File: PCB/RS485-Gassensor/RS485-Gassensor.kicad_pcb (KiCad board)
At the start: 2 copper layers, 92 x 46 mm, 66 parts, among them J1 Screw_Terminal_01x08, J2 Screw_Terminal_01x04, J3 Screw_Terminal_01x08, J4 Screw_Terminal_01x06, J5 Screw_Terminal_01x06, SW1 SW_DIP_x06, U1 STM32G031K8Tx, U2 STM32G031K8Ux, U3 MQ-6, U4 OKI-78SR-5_1.5-W36-C, U5 AP2127N-3.3, U6 AD8676xR, U7 LT1785xS8, U8 MQ-6, U9 AD8676xR

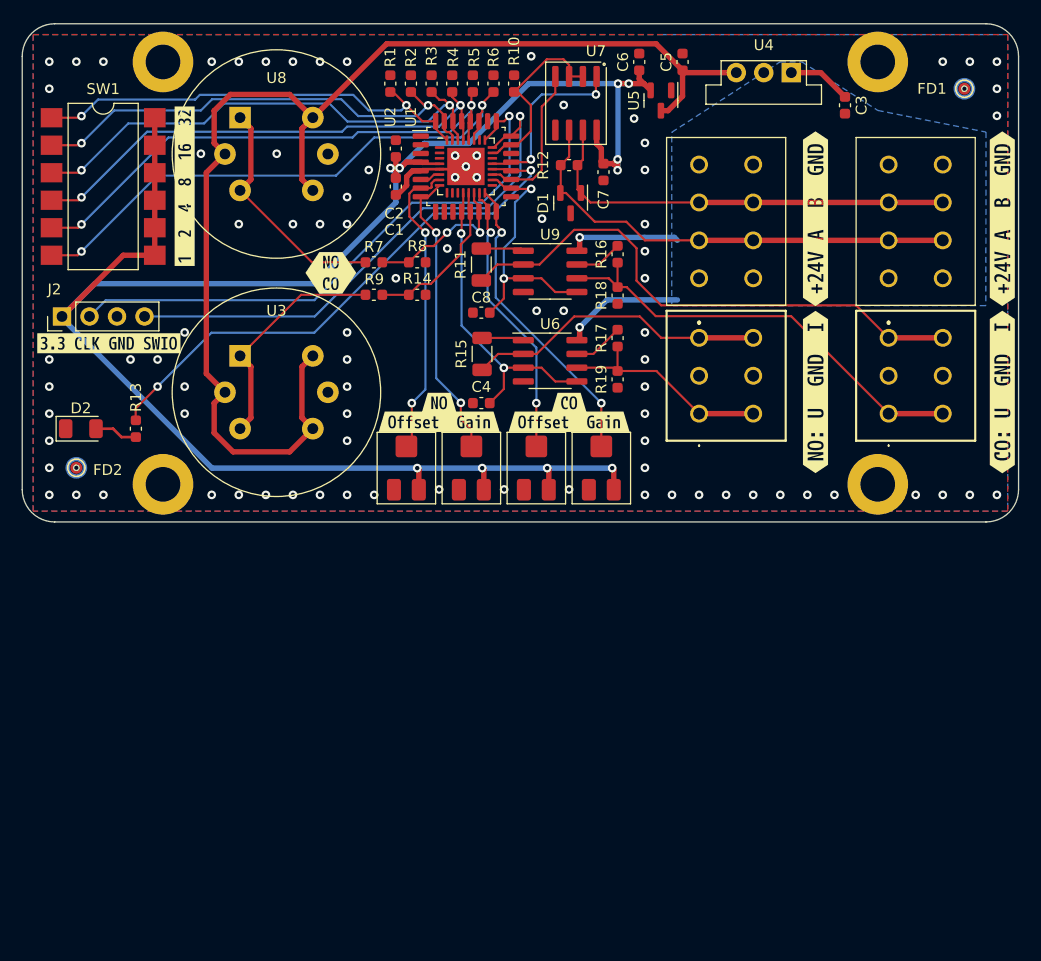
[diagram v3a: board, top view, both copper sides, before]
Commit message: imoproved filter
one dual channel Op amp, corrections from first produced prototype
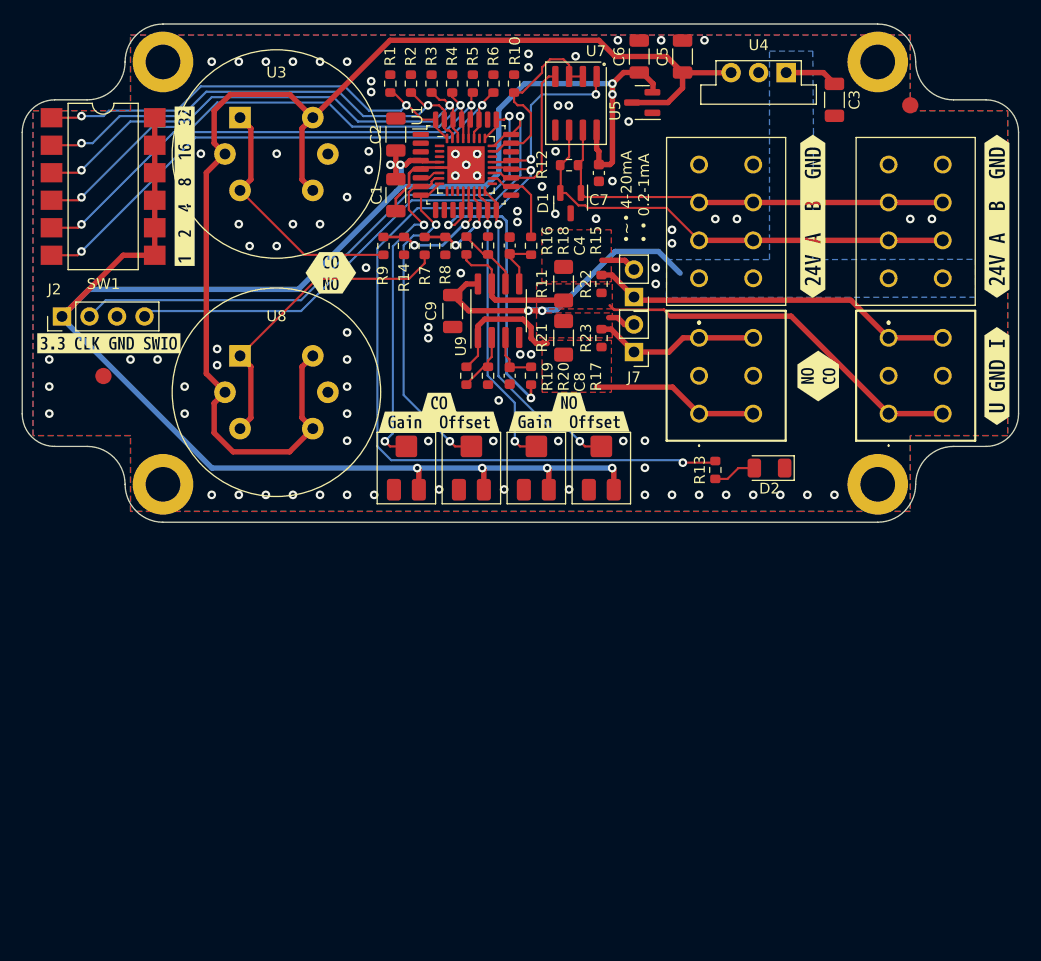
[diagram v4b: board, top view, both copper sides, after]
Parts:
- removed FD1, FD2: ~, Custom_Library:Alignement_Testpoint_2Layer
- removed U6: AD8676xR, Package_SO:SOIC-8_3.9x4.9mm_P1.27mm
- removed kibuzzard-64E927CD: G***, kibuzzard-64E927CD
- removed kibuzzard-64E9307C (x2): G***, kibuzzard-64E9307C
- removed kibuzzard-64E930E3: G***, kibuzzard-64E930E3
- removed kibuzzard-64E93122: G***, kibuzzard-64E93122
- removed kibuzzard-64E95911 (x2): G***, kibuzzard-64E95911
- added C9: CAP1uF, Capacitor_SMD:C_1206_3216Metric, F.Cu at (169.8, 45.5)
- added FID1: Fiducial, Fiducial:Fiducial_1.5mm_Mask3mm, F.Cu at (137.5, 51.5)
- added FID2: Fiducial, Fiducial:Fiducial_1.5mm_Mask3mm, F.Cu at (212.0, 26.5)
- added J6: Conn_01x02_Pin, Connector_PinHeader_2.54mm:PinHeader_1x02_P2.54mm_Vertical, F.Cu at (186.5, 44.2)
- added J7: Conn_01x02_Pin, Connector_PinHeader_2.54mm:PinHeader_1x02_P2.54mm_Vertical, F.Cu at (186.5, 49.3)
- added R20: R1K, Resistor_SMD:R_0603_1608Metric, F.Cu at (173.0, 51.5)
- added R21: R470, Resistor_SMD:R_1206_3216Metric_Pad1.30x1.75mm_HandSolder, F.Cu at (180.0, 48.0)
- added R22: 10KR, Resistor_SMD:R_0603_1608Metric, F.Cu at (183.5, 43.0)
- added R23: 10KR, Resistor_SMD:R_0603_1608Metric, F.Cu at (183.5, 48.0)
- added kibuzzard-64EB9F88: G***, kibuzzard-64EB9F88, F.Cu at (158.5, 42.0)
- added kibuzzard-64ECCA5B: G***, kibuzzard-64ECCA5B, F.Cu at (203.0, 36.8)
- added kibuzzard-64ECCA80: G***, kibuzzard-64ECCA80, F.Cu at (220.0, 36.8)
- added kibuzzard-64ECCBAE: G***, kibuzzard-64ECCBAE, F.Cu at (220.0, 51.5)
- added kibuzzard-650224BF: G***, kibuzzard-650224BF, F.Cu at (168.5, 55.7)
- added kibuzzard-650224CC: G***, kibuzzard-650224CC, F.Cu at (180.5, 55.7)
- added kibuzzard-650224F1: G***, kibuzzard-650224F1, F.Cu at (203.5, 51.5)
- C1, C2, C6: footprint Capacitor_SMD:C_0603_1608Metric -> Capacitor_SMD:C_1206_3216Metric
- C3: value CAP2.2uF -> CAP10uF; footprint Capacitor_SMD:C_0603_1608Metric -> Capacitor_SMD:C_1206_3216Metric
- C4, C8: value CAP100nF -> 470nF
- C5: value CAP2.2uF -> CAP22uF; footprint Capacitor_SMD:C_0603_1608Metric -> Capacitor_SMD:C_1206_3216Metric
- R1, R10, R12, R13, R14, R18, R2, R3, R4, R5, R6, R7, R8, R9: footprint Capacitor_SMD:C_0603_1608Metric -> Resistor_SMD:R_0603_1608Metric
- R11: value R150 -> R470; footprint Capacitor_SMD:C_1206_3216Metric -> Resistor_SMD:R_1206_3216Metric_Pad1.30x1.75mm_HandSolder
- R15: value R150 -> 1k; footprint Capacitor_SMD:C_1206_3216Metric -> Resistor_SMD:R_0603_1608Metric
- R16, R19: value R1K -> 2.2k; footprint Capacitor_SMD:C_0603_1608Metric -> Resistor_SMD:R_0603_1608Metric
- R17: value R1K -> 1k; footprint Capacitor_SMD:C_0603_1608Metric -> Resistor_SMD:R_0603_1608Metric
- U9: value AD8676xR -> AD8676
- moved D2 63.7 mm to (199.0, 60.0), turned to 180 degrees
- moved R13 53.6 mm to (194.0, 60.2)
- moved U3 22.0 mm to (150.1, 27.6)
- moved U8 22.0 mm to (150.1, 49.6)
- moved C4 14.8 mm to (175.0, 39.4), turned to 90 degrees
- moved R16 14.0 mm to (171.0, 39.4), turned to 90 degrees
- moved R19 14.0 mm to (171.0, 51.5)
- moved R18 12.8 mm to (173.0, 39.4), turned to 90 degrees
- moved kibuzzard-64E958EB 12.0 mm to (180.5, 54.0)
- moved kibuzzard-64E958FD 12.0 mm to (168.5, 54.0)
- moved R15 11.0 mm to (177.0, 39.5)
- moved R17 8.71 mm to (177.0, 51.5), turned to 90 degrees
- moved R11 7.80 mm to (180.0, 43.0), turned to 90 degrees
- moved C8 6.39 mm to (175.0, 51.5), turned to -90 degrees
- moved U9 5.99 mm to (174.0, 45.5), turned to 90 degrees
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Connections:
- net /CO renamed CO
- net /DIP0 renamed DIP0
- net /DIP1 renamed DIP1
- net /DIP2 renamed DIP2
- net /DIP3 renamed DIP3
- net /DIP4 renamed DIP4
- net /DIP5 renamed DIP5
- net /Gain_CO renamed Gain_CO
- net /Gain_NO renamed Gain_NO
- net /LED renamed LED
- net /NO2 renamed NO2
- net /RS485-A renamed RS485-A
- net /RS485-B renamed RS485-B
- net /Read_!Enable renamed Read_!Enable
- net /SWCLK renamed SWCLK
- net /SWDIO renamed SWDIO
- net /T_NRST-Button renamed T_NRST-Button
- net /UART_RX renamed UART_RX
- net /UART_TX renamed UART_TX
- net /offset_CO renamed offset_CO
- net /offset_NO renamed offset_NO
- C4 pad 1: /analog_PWM_NO -> Net-(U9B-+)
- C8 pad 1: /analog_PWM_CO -> Net-(U9A-+)
- J4 pad 1: /U_Out_NO -> U_Out_NO
- J4 pad 2: /U_Out_NO -> U_Out_NO
- J4 pad 5: /I_Out_NO -> I_Out_NO
- J4 pad 6: /I_Out_NO -> I_Out_NO
- J5 pad 1: /U_Out_CO -> U_Out_CO
- J5 pad 2: /U_Out_CO -> U_Out_CO
- J5 pad 5: /I_Out_CO -> I_Out_CO
- J5 pad 6: /I_Out_CO -> I_Out_CO
- R11 pad 1: Net-(R11-Pad1) -> U_Out_CO
- R11 pad 2: /I_Out_CO -> Net-(J6-Pin_2)
- R15 pad 1: Net-(R15-Pad1) -> analog_PWM_CO
- R15 pad 2: /I_Out_NO -> Net-(U9B-+)
- R16 pad 1: Net-(R16-Pad1) -> U_Out_CO
- R16 pad 2: /U_Out_CO -> Net-(U9B--)
- R17 pad 1: Net-(R17-Pad1) -> analog_PWM_NO
- R17 pad 2: /U_Out_NO -> Net-(U9A-+)
- R18 pad 1: /U_Out_CO -> Net-(U9B--)
- R19 pad 1: /U_Out_NO -> U_Out_NO
- R19 pad 2: GND -> Net-(U9A--)
- U1 pad 12: /analog_PWM_NO -> analog_PWM_NO
- U1 pad 18: /analog_PWM_CO -> analog_PWM_CO
- U2 pad 12: /analog_PWM_NO -> analog_PWM_NO
- U2 pad 18: /analog_PWM_CO -> analog_PWM_CO
- U9 pad 1: Net-(R11-Pad1) -> U_Out_NO
- U9 pad 2: /I_Out_CO -> Net-(U9A--)
- U9 pad 3: /analog_PWM_CO -> Net-(U9A-+)
- U9 pad 5: /analog_PWM_CO -> Net-(U9B-+)
- U9 pad 6: /U_Out_CO -> Net-(U9B--)
- U9 pad 7: Net-(R16-Pad1) -> U_Out_CO
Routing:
- net /I_Out_CO: track 50.4 -> 0.00 mm
- net U_Out_CO: track 0.00 -> 47.5 mm
- net /U_Out_CO: track 41.2 -> 0.00 mm
- net I_Out_CO: track 0.00 -> 33.9 mm
- net /analog_PWM_NO: track 28.9 -> 0.00 mm, vias 2 -> 0
- net analog_PWM_NO: track 0.00 -> 28.4 mm, vias 0 -> 2
- net U_Out_NO: track 0.00 -> 28.0 mm
- net /I_Out_NO: track 27.9 -> 0.00 mm
- net /analog_PWM_CO: track 24.4 -> 0.00 mm, vias 2 -> 0
- net LED: track 50.6 -> 71.2 mm
- net /U_Out_NO: track 20.3 -> 0.00 mm
- net I_Out_NO: track 0.00 -> 15.4 mm
- net analog_PWM_CO: track 0.00 -> 7.51 mm
- net Net-(U8-B1): track 21.9 -> 28.9 mm
- net Net-(U9B--): track 0.00 -> 6.08 mm
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- added copper zone on F.Cu, net Net-(J6-Pin_2)
- added copper zone on F.Cu, net Net-(J7-Pin_2)
- added copper zone on F.Cu, net U_Out_CO
- added copper zone on F.Cu, net U_Out_NO
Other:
- outline, holes or cut-outs redrawn
- board text added: "PROTOTYPE V2 Garage Gas Sensor Felix Sarbach 2023"
- board text added: "•~• 4-20mA • • 0.2-1mA"
- board text removed: "PROTOTYPE V1 Garage Gas Sensor Felix Sarbach 2023"

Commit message: added Modbus / RS485
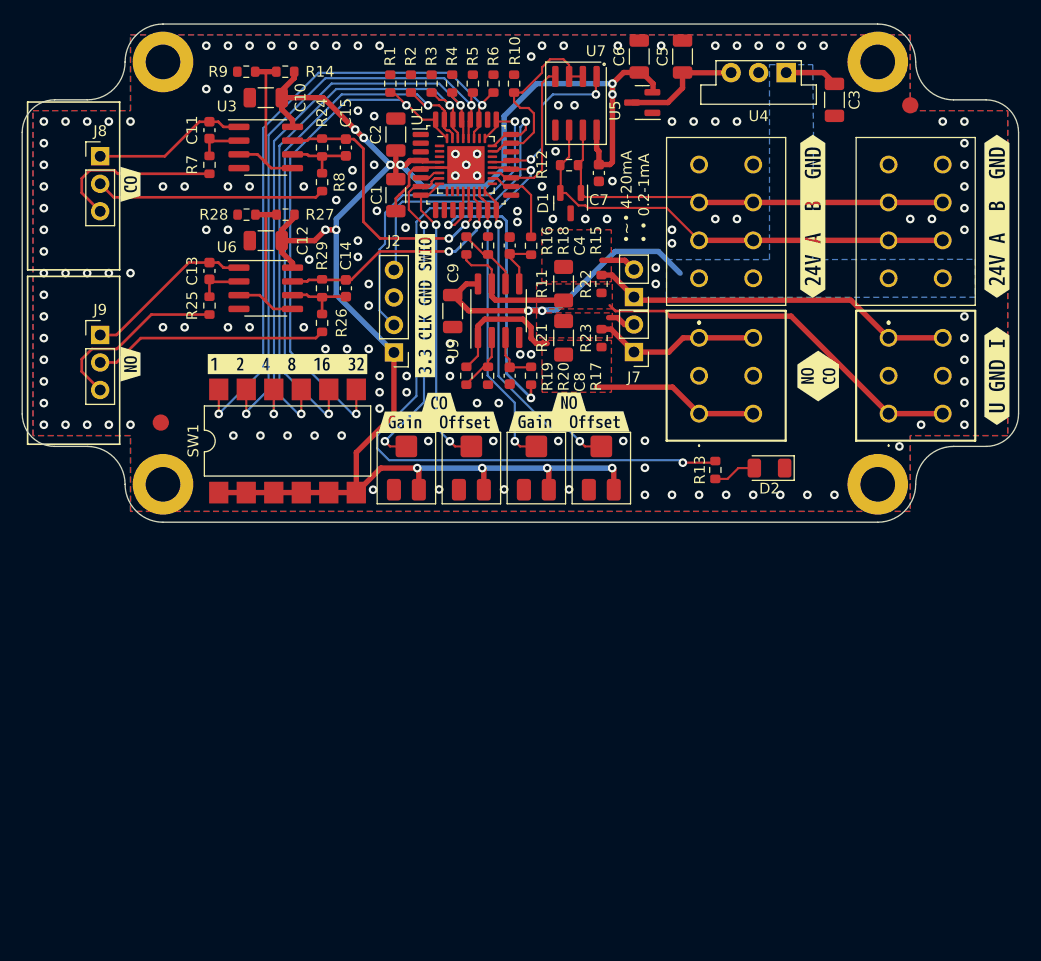
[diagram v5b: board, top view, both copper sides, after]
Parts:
- removed U8: MQ-6, Sensor:MQ-6
- removed kibuzzard-64EB9F88: G***, kibuzzard-64EB9F88
- added C10: CAP1uF, Capacitor_SMD:C_1206_3216Metric, F.Cu at (152.5, 25.8)
- added C11: CAP1uF, Capacitor_SMD:C_0603_1608Metric, F.Cu at (147.3, 28.8)
- added C12: CAP1uF, Capacitor_SMD:C_1206_3216Metric, F.Cu at (152.5, 39.0)
- added C13: CAP1uF, Capacitor_SMD:C_0603_1608Metric, F.Cu at (147.3, 41.8)
- added C14: CAP1uF, Capacitor_SMD:C_0603_1608Metric, F.Cu at (159.9, 43.4)
- added C15: CAP1uF, Capacitor_SMD:C_0603_1608Metric, F.Cu at (159.9, 30.4)
- added J8: Conn_01x03, Connector_PinHeader_2.54mm:PinHeader_1x03_P2.54mm_Vertical, F.Cu at (137.2, 31.2)
- added J9: Conn_01x03, Connector_PinHeader_2.54mm:PinHeader_1x03_P2.54mm_Vertical, F.Cu at (137.2, 47.7)
- added R24: R10K, Resistor_SMD:R_0603_1608Metric, F.Cu at (157.7, 30.4)
- added R25: R10K, Resistor_SMD:R_0603_1608Metric, F.Cu at (147.3, 45.0)
- added R26: 10, Resistor_SMD:R_0603_1608Metric, F.Cu at (157.7, 46.6)
- added R27: 2.2k, Resistor_SMD:R_0603_1608Metric, F.Cu at (154.3, 36.6)
- added R28: 1k, Resistor_SMD:R_0603_1608Metric, F.Cu at (150.7, 36.6)
- added R29: R10K, Resistor_SMD:R_0603_1608Metric, F.Cu at (157.7, 43.4)
- added U6: MCP6002-xMS, Package_SO:SOIC-8_3.9x4.9mm_P1.27mm, F.Cu at (152.5, 43.4)
- added kibuzzard-651DD8EE: G***, kibuzzard-651DD8EE, F.Cu at (140.0, 50.4)
- added kibuzzard-651DD908: G***, kibuzzard-651DD908, F.Cu at (140.0, 33.8)
- R14: value R1K -> 2.2k
- R7: value 470R -> R10K
- R8: value R1K -> 10
- R9: value 470R -> 1k
- U3: value MQ-6 -> MCP6002-xMS; footprint Sensor:MQ-6 -> Package_SO:SOIC-8_3.9x4.9mm_P1.27mm
- moved J2 30.8 mm to (164.4, 49.3), turned to 180 degrees
- moved kibuzzard-64E925B6 29.4 mm to (167.2, 45.0), turned to 90 degrees
- moved SW1 29.0 mm to (154.5, 57.5), turned to 90 degrees
- moved R7 21.2 mm to (147.3, 32.0)
- moved R9 20.5 mm to (150.7, 23.4), turned to 0 degrees
- moved R14 19.5 mm to (154.3, 23.4), turned to 0 degrees
- moved G*** 19.4 mm to (150.0, 35.0)
- moved kibuzzard-64E92756 19.0 mm to (154.5, 50.4), turned to 0 degrees
- moved R8 12.8 mm to (157.7, 33.6)
- moved FID1 6.82 mm to (142.8, 55.8)
- moved U3 3.64 mm to (152.5, 30.4)
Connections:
- R14 pad 1: GND -> Net-(U3A-+)
- R14 pad 2: CO -> +3.3V
- R7 pad 1: Net-(U8-B1) -> /Inputs and sensors/Reference_CO
- R7 pad 2: NO2 -> Net-(U3A--)
- R8 pad 1: GND -> /Inputs and sensors/Working_CO
- R8 pad 2: NO2 -> Net-(U3B--)
- R9 pad 1: Net-(U3-B1) -> GND
- R9 pad 2: CO -> Net-(U3A-+)
- SW1 pad 1: DIP0 -> +3.3V
- SW1 pad 10: +3.3V -> DIP3
- SW1 pad 11: +3.3V -> DIP4
- SW1 pad 12: +3.3V -> DIP5
- SW1 pad 2: DIP1 -> +3.3V
- SW1 pad 3: DIP2 -> +3.3V
- SW1 pad 4: DIP3 -> +3.3V
- SW1 pad 5: DIP4 -> +3.3V
- SW1 pad 6: DIP5 -> +3.3V
- SW1 pad 7: +3.3V -> DIP0
- SW1 pad 8: +3.3V -> DIP1
- SW1 pad 9: +3.3V -> DIP2
- U3 pad 1: Net-(U3-B1) -> /Inputs and sensors/Counter_CO
- U3 pad 2: +5V -> Net-(U3A--)
- U3 pad 3: Net-(U3-B1) -> Net-(U3A-+)
- U3 pad 4: +5V -> GND
- U3 pad 5: GND -> Net-(U3A-+)
- U3 pad 6: +5V -> Net-(U3B--)
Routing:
- net +5V: track 117.9 -> 11.1 mm
- net Net-(U8-B1): track 28.9 -> 0.00 mm
- net Net-(U3-B1): track 23.3 -> 0.00 mm
- net /Inputs and sensors/Working_NO: track 0.00 -> 21.7 mm
- net SWDIO: track 49.8 -> 28.2 mm
- net /Inputs and sensors/Working_CO: track 0.00 -> 21.2 mm
- net SWCLK: track 53.2 -> 33.2 mm
- net /Inputs and sensors/Reference_NO: track 0.00 -> 17.0 mm
- net Net-(U3A-+): track 0.00 -> 16.0 mm
- net /Inputs and sensors/Reference_CO: track 0.00 -> 16.0 mm
- net /Inputs and sensors/Counter_NO: track 0.00 -> 15.8 mm
- net Net-(U6A-+): track 0.00 -> 15.4 mm
- net CO: track 12.0 -> 27.4 mm
- net /Inputs and sensors/Counter_CO: track 0.00 -> 14.3 mm
- net NO2: track 9.28 -> 22.8 mm
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
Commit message: made For NAP505 and NAP550
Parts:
- added C16: CAP100nF, Capacitor_SMD:C_0603_1608Metric, F.Cu at (145.0, 28.7)
- added J10: Conn_01x02, Connector_PinHeader_2.54mm:PinHeader_1x02_P2.54mm_Vertical, F.Cu at (161.3, 21.8)
- added R30: R10K, Resistor_SMD:R_0603_1608Metric, F.Cu at (158.8, 24.8)
- added R31: R10K, Resistor_SMD:R_0603_1608Metric, F.Cu at (161.3, 24.8)
- added U8: SHT4x, Sensor_Humidity:Sensirion_DFN-4_1.5x1.5mm_P0.8mm_SHT4x_NoCentralPad, F.Cu at (142.3, 28.8)
- C1: value CAP4.7nF -> CAP4.7uF
- R27: value 2.2k -> 1k
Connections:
- U1 pad 1: unconnected-(U1-PB9-Pad1) -> I2C_SDA
- U1 pad 2: unconnected-(U1-PC14-Pad2) -> DIP0
- U1 pad 30: DIP2 -> I2C_SCL
- U1 pad 31: DIP1 -> DIP2
- U1 pad 32: DIP0 -> DIP1
- U2 pad 1: unconnected-(U2-PB9-Pad1) -> I2C_SDA
- U2 pad 2: unconnected-(U2-PC14-Pad2) -> DIP0
- U2 pad 30: DIP2 -> I2C_SCL
- U2 pad 31: DIP1 -> DIP2
- U2 pad 32: DIP0 -> DIP1
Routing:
- net I2C_SCL: track 0.00 -> 44.3 mm
- net I2C_SDA: track 0.00 -> 38.4 mm
- net +3.3V: track 169.7 -> 192.1 mm
- net GND: track 10.0 -> 21.7 mm, vias 154 -> 157
- net DIP2: track 52.3 -> 50.0 mm
- net DIP1: track 51.6 -> 49.4 mm
- net /Inputs and sensors/Counter_CO: track 14.3 -> 15.4 mm
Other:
- board text added: "I2C SDA SCL"
- board text added: "PROTOTYPE V2 Garage Gas Sensor Felix Sarbach 2024"
- board text removed: "PROTOTYPE V2 Garage Gas Sensor Felix Sarbach 2023"
